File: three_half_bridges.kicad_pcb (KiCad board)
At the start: 2 copper layers, 100 x 100 mm, 167 parts, among them J1 Conn_01x06_Pin, J2 Conn_01x06_Pin, J3 Conn_01x06_Pin, J4 Current Sense, J5 Conn_01x01_Socket, J6 Conn_01x01_Socket, J7 Conn_01x01_Socket, J8 Conn_01x01_Socket, J9 Conn_01x01_Socket, Q1 Q_NMOS_GDS, Q2 Q_NMOS_GDS, Q3 Q_NIGBT_GCE, Q4 Q_NIGBT_GCE, Q5 Q_NIGBT_GCE, Q6 Q_NIGBT_GCE, Q7 Q_NIGBT_GCE, Q8 Q_NIGBT_GCE, U1 ACS730xLCTR-50AB, U10 ADuM121N, U13 EL7202CN, U14 EL7202CN, U15 EL7202CN, U16 EL7202CN, U17 ACS730xLCTR-50AB, U18 ADuM121N, U19 ADuM121N, U2 ACS730xLCTR-50AB, U22 EL7202CN, U23 EL7202CN, U3 SN6505BDBV, U4 ADuM121N, U5 ADuM121N, U9 ADuM121N

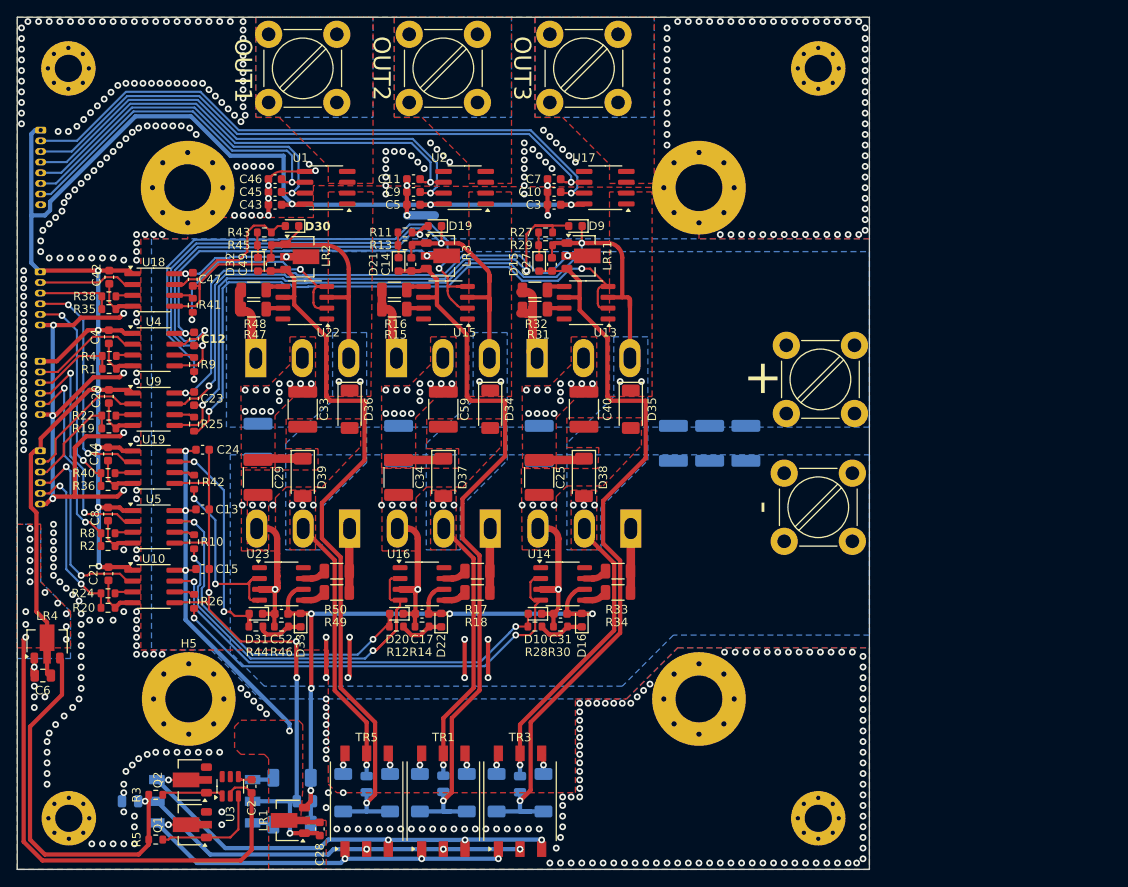
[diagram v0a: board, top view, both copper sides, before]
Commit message: Updated LDO footrprint to use the SOT89 LM78L05 (issue 10); moved high side local regulators closer to digital isolator ICs (issue 10); pushed digital isolator ICs further to the allow room for LRs (issue 10); changed designator letter for zener diodes to Z to make it easier when hand soldering (issue 5) Updated footprints from placeholders (most of the diodes) to actual real component choices updated resistor values for BOM consolidation (220, 1k) moved resistor related to PGOOD for more optimal routing w/ minimal impact to function Changed structure of isolated driver design to use voltage doubler and 6505 or similar IC directly (issue 7,8,13) Only 5VDC is required for low voltage side, although several amps may be required depending on gate drive requirements Updated transformer footprint for more common 7.5mm by 2.5mm spacing, several 1:1.1 to 1:1.5 transformers are avilable with such spacing (issue 7) Moved Q8 designator back to correct place along with others that were mislocated somehow... Fixed placement of some footprints that were slightly off or not aligned to 0.25mm grid Replaced specific SO8 MOSFET driver with choose-your-own generic. I am personally using some cheapo LCSC TI 27523 clones (issue 11) added EVEN MORE VIAS!!!! thermal vias on not current sensitive pins to make soldering easier Added artwork (issue 6)
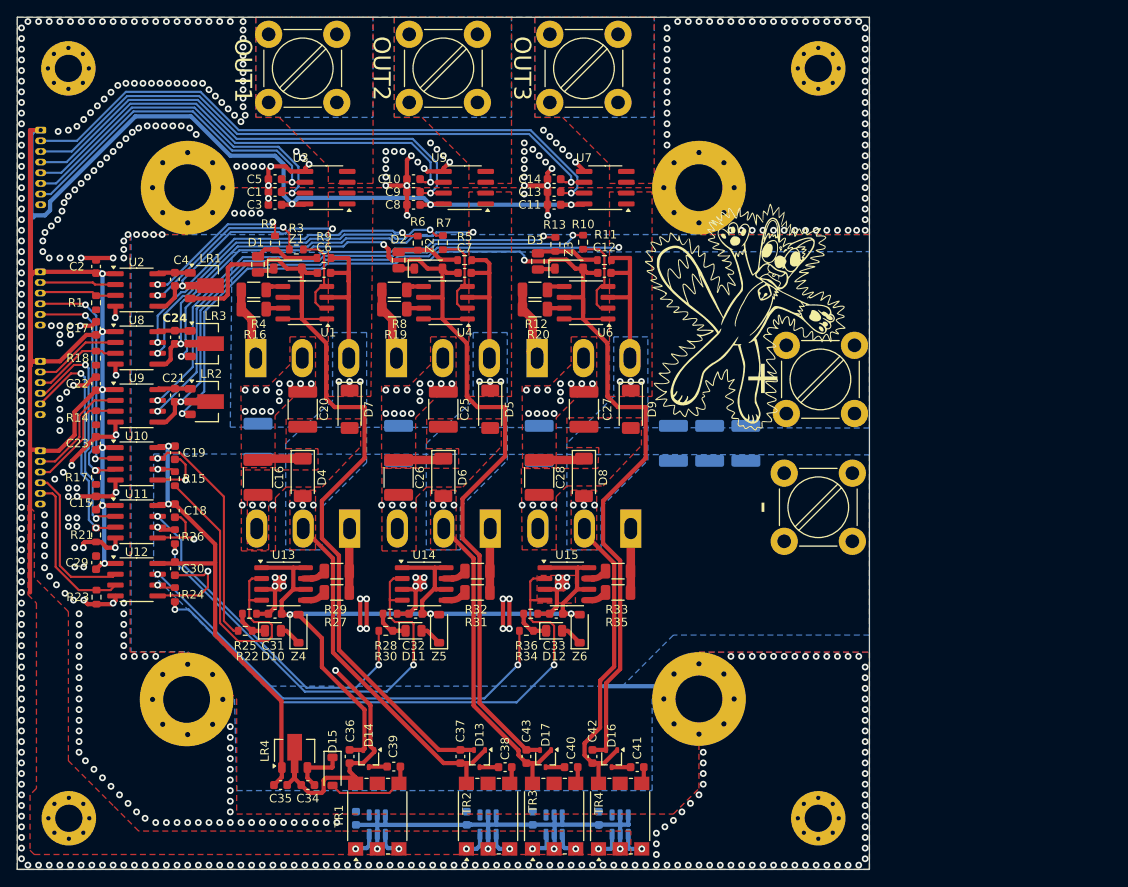
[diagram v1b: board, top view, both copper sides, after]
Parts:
- removed the C1 at (93.2, 122.0)
- removed the C16 at (130.0, 120.0)
- removed the C2 at (107.5, 120.2)
- removed the C26 at (113.8, 122.0)
- removed the C28 at (115.5, 125.2)
- removed the C30 at (139.0, 120.0)
- removed the C6 at (83.0, 107.2)
- removed D18, D28, D29: 1N4148WT, Diode_SMD:D_SOD-128
- removed the D7 at (112.2, 124.8)
- removed the D8 at (112.2, 119.2)
- removed LR11: AMS1117-5.0, Package_TO_SOT_SMD:SOT-89-3
- removed the Q1 at (100.2, 124.8)
- removed the Q2 at (100.2, 119.5)
- removed the R22 at (90.8, 76.8)
- removed the R24 at (90.7, 97.6)
- removed the R3 at (96.2, 121.2)
- removed R38, R40: 470, Resistor_SMD:R_0603_1608Metric
- removed the R4 at (90.8, 69.8)
- removed the R5 at (96.2, 126.5)
- removed the R8 at (90.7, 90.5)
- removed the TR2 at (102.0, 122.0)
- removed U23: EL7202CN, Package_SO:SO-8_3.9x4.9mm_P1.27mm
- removed the U3 at (105.0, 120.2)
- added C34: 1u, Capacitor_SMD:C_0603_1608Metric, F.Cu at (114.1, 120.1)
- added C35: 1u, Capacitor_SMD:C_0603_1608Metric, F.Cu at (110.9, 120.1)
- added C36: 1u, Capacitor_SMD:C_0603_1608Metric, F.Cu at (119.0, 116.8)
- added C37: 1u, Capacitor_SMD:C_0603_1608Metric, F.Cu at (132.0, 116.8)
- added C38: 1u, Capacitor_SMD:C_0603_1608Metric, F.Cu at (137.2, 118.0)
- added C39: 1u, Capacitor_SMD:C_0603_1608Metric, F.Cu at (124.2, 117.9)
- added C40: 1u, Capacitor_SMD:C_0603_1608Metric, F.Cu at (145.0, 118.0)
- added C41: 1u, Capacitor_SMD:C_0603_1608Metric, F.Cu at (152.8, 118.0)
- added C42: 1u, Capacitor_SMD:C_0603_1608Metric, F.Cu at (147.5, 116.8)
- added C43: 1u, Capacitor_SMD:C_0603_1608Metric, F.Cu at (139.8, 116.8)
- added C50: 1u, Capacitor_SMD:C_0603_1608Metric, B.Cu at (140.5, 124.0)
- added C52: 1u, Capacitor_SMD:C_0603_1608Metric, B.Cu at (119.8, 124.0)
- added C53: 1u, Capacitor_SMD:C_0603_1608Metric, B.Cu at (132.8, 124.0)
- added D15: D_Schottky, Diode_SMD:D_SOD-123, F.Cu at (117.0, 118.5)
- added D16: BAT54SW, Package_TO_SOT_SMD:SOT-323_SC-70, F.Cu at (149.8, 117.0)
- added G***: LOGO, PM art:PM_art, F.Cu at (165.6, 65.2)
- added TR1: EPC3668G, Transformer_SMD:Pulse_PA2004NL, F.Cu at (122.2, 123.8)
- added U13: SO8 GATE DRVR, Package_SO:SO-8_3.9x4.9mm_P1.27mm, F.Cu at (111.2, 96.5)
- added U15: SO8 GATE DRVR, Package_SO:SO-8_3.9x4.9mm_P1.27mm, F.Cu at (144.5, 96.5)
- added U17: SN6505BDBV, Package_TO_SOT_SMD:SOT-23-6, B.Cu at (150.8, 124.8)
- added U18: SN6505BDBV, Package_TO_SOT_SMD:SOT-23-6, B.Cu at (135.2, 124.8)
- added U19: SN6505BDBV, Package_TO_SOT_SMD:SOT-23-6, B.Cu at (122.2, 124.8)
- C1: renamed from C45; value 100n -> 1n
- C10: renamed from C11; value 100n -> 1n
- C12: renamed from C27; value 100n -> 1u
- C13: renamed from C10; value 100n -> 1n
- C14: renamed from C7; value 100n -> 1n
- C16: renamed from C29; value 100n -> 470n
- C20: renamed from C33; value 100n -> 470n
- C25: renamed from C59; value 100n -> 470n
- C26: renamed from C34; value 100n -> 470n
- C27: renamed from C40; value 100n -> 470n
- C28: renamed from C25; value 100n -> 470n
- C5: renamed from C46; value 100n -> 1n
- C51: value 10u -> 1u; footprint Capacitor_SMD:C_0805_2012Metric -> Capacitor_SMD:C_0603_1608Metric
- C6: renamed from C49; value 100n -> 1u
- C7: renamed from C14; value 100n -> 1u
- C9: value 100n -> 1n
- D1: renamed from D30; footprint LED_SMD:LED_0603_1608Metric -> Capacitor_SMD:C_0805_2012Metric
- D10: renamed from D31; footprint LED_SMD:LED_0603_1608Metric -> LED_SMD:LED_0805_2012Metric
- D11: renamed from D20; footprint LED_SMD:LED_0603_1608Metric -> LED_SMD:LED_0805_2012Metric
- D12: renamed from D10; footprint LED_SMD:LED_0603_1608Metric -> LED_SMD:LED_0805_2012Metric
- D13, D14, D17: value 1N4148WT -> BAT54SW; footprint Diode_SMD:D_SOD-128 -> Package_TO_SOT_SMD:SOT-323_SC-70; moved to F.Cu
- D2: renamed from D19; footprint LED_SMD:LED_0603_1608Metric -> Capacitor_SMD:C_0805_2012Metric
- D3: renamed from D9; footprint LED_SMD:LED_0603_1608Metric -> Capacitor_SMD:C_0805_2012Metric
- D4: renamed from D39; value 1N4148WT -> FAST 1A DIODE
- D5: renamed from D34; value 1N4148WT -> FAST 1A DIODE
- D6: renamed from D37; value 1N4148WT -> FAST 1A DIODE
- D7: renamed from D36; value 1N4148WT -> FAST 1A DIODE
- D8: renamed from D38; value 1N4148WT -> FAST 1A DIODE
- D9: renamed from D35; value 1N4148WT -> FAST 1A DIODE
- LR1, LR2, LR3, LR4: value AMS1117-5.0 -> MC78L08_SOT89
- R1: renamed from R35; value 10k -> 1k
- R11: renamed from R27; value 4.7k -> 1k
- R14: renamed from R19; value 10k -> 1k
- R17: renamed from R36; value 10k -> 1k
- R18: renamed from R1; value 10k -> 1k
- R21: renamed from R2; value 10k -> 1k
- R23: renamed from R20; value 10k -> 1k
- R25: renamed from R44; value 4.7k -> 1k
- R30: renamed from R12; value 4.7k -> 1k
- R34: renamed from R28; value 4.7k -> 1k
- R5: renamed from R11; value 4.7k -> 1k
- R9: renamed from R43; value 4.7k -> 1k
- TR2: renamed from TR5; value Wuerth_750315371 -> EPC3668G; footprint Transformer_SMD:Transformer_Wuerth_750315371 -> Transformer_SMD:Pulse_PA2004NL
- TR3: renamed from TR1; value Wuerth_750315371 -> EPC3668G; footprint Transformer_SMD:Transformer_Wuerth_750315371 -> Transformer_SMD:Pulse_PA2004NL
- TR4: renamed from TR3; value Wuerth_750315371 -> EPC3668G; footprint Transformer_SMD:Transformer_Wuerth_750315371 -> Transformer_SMD:Pulse_PA2004NL
- U1: renamed from U22; value EL7202CN -> SO8 GATE DRVR
- U14: value EL7202CN -> SO8 GATE DRVR
- U16: value EL7202CN -> SN6505BDBV; footprint Package_SO:SO-8_3.9x4.9mm_P1.27mm -> Package_TO_SOT_SMD:SOT-23-6; moved to B.Cu
- U4: renamed from U15; value EL7202CN -> SO8 GATE DRVR
- U6: renamed from U13; value EL7202CN -> SO8 GATE DRVR
- Z1: renamed from D32; footprint Diode_SMD:D_0603_1608Metric -> Diode_SMD:D_SOD-123
- Z2: renamed from D21; footprint Diode_SMD:D_0603_1608Metric -> Diode_SMD:D_SOD-123
- Z3: renamed from D15; footprint Diode_SMD:D_0603_1608Metric -> Diode_SMD:D_SOD-123
- Z4: renamed from D33; footprint Diode_SMD:D_0603_1608Metric -> Diode_SMD:D_SOD-123
- Z5: renamed from D22; footprint Diode_SMD:D_0603_1608Metric -> Diode_SMD:D_SOD-123
- Z6: renamed from D16; footprint Diode_SMD:D_0603_1608Metric -> Diode_SMD:D_SOD-123
- moved LR1 63.5 mm to (102.2, 61.5), turned to 0 degrees
- moved R10 50.4 mm to (146.4, 56.4)
- moved R7 32.5 mm to (129.9, 56.5)
- moved U16 32.2 mm to (143.0, 124.8), turned to 90 degrees
- moved LR4 31.8 mm to (112.5, 116.1)
- moved LR3 29.6 mm to (102.2, 68.3)
- moved C51 27.5 mm to (148.2, 124.0)
- moved D14 20.9 mm to (121.2, 117.0), turned to -90 degrees
- moved LR2 20.3 mm to (102.2, 75.1)
- moved U14 16.2 mm to (127.8, 96.5)
- moved D17 15.3 mm to (142.0, 117.0), turned to -90 degrees
- moved TR2 14.4 mm to (135.2, 123.8)
- moved R3 13.8 mm to (112.8, 57.2), turned to 180 degrees
- moved TR3 13.1 mm to (143.0, 123.8)
- moved TR4 11.9 mm to (150.8, 123.8)
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- renumbered C3 to C11, C8 to C15, C4 to C17, C13 to C18, C24 to C19, C42 to C2, C23 to C21, C20 to C22, C44 to C23, C12 to C24, C21 to C29, C43 to C3, C15 to C30, C52 to C31, C17 to C32, C31 to C33, C47 to C4, C18 to C44, C19 to C45, C32 to C46, C22 to C47, C35 to C48, C36 to C49, C5 to C8, J9 to J1, J8 to J2, J7 to J3, J5 to J4, J6 to J5, J4 to J6, J3 to J7, J2 to J8, J1 to J9, Q5 to Q1, Q3 to Q2, Q7 to Q3, Q6 to Q4, Q4 to Q5, Q8 to Q6, R25 to R10, R32 to R12, R29 to R13, R42 to R15, R47 to R16, R15 to R19, R45 to R2, R31 to R20, R46 to R22, R26 to R24, R10 to R26, R49 to R27, R14 to R28, R50 to R29, R41 to R3, R18 to R31, R17 to R32, R34 to R35, R30 to R36, R48 to R4, R13 to R6, R9 to R7, R16 to R8, U19 to U10, U5 to U11, U10 to U12, U18 to U2, U1 to U3, U2 to U5, U17 to U7, U4 to U8
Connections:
- C12 pad 1: Net-(D13-K) -> Net-(D3-K)
- C12 pad 2: Net-(D35-K) -> /half bridge 1/SWNODE
- C21 pad 1: Net-(LR11-VO) -> Net-(LR11-OUT)
- C21 pad 2: Net-(D35-K) -> /half bridge 1/SWNODE
- C24 pad 1: Net-(LR3-VO) -> Net-(LR8-OUT)
- C24 pad 2: Net-(D19-K) -> /half bridge 2/SWNODE
- C4 pad 1: Net-(LR2-VO) -> Net-(LR12-OUT)
- C4 pad 2: Net-(D30-K) -> /half bridge 3/SWNODE
- C51 pad 1: Net-(D30-K) -> GND
- C51 pad 2: Net-(D28-K) -> +5V
- C6 pad 1: Net-(D28-K) -> Net-(D4-K)
- C6 pad 2: Net-(D30-K) -> /half bridge 3/SWNODE
- C7 pad 1: Net-(D17-K) -> Net-(D2-K)
- C7 pad 2: Net-(D19-K) -> /half bridge 2/SWNODE
- D10 pad 1: -VDC -> Net-(D31-K)
- D11 pad 1: -VDC -> Net-(D20-K)
- D12 pad 1: -VDC -> Net-(D10-K)
- D13 pad 1: Net-(D13-K) -> /half bridge 3/SWNODE
- D13 pad 2: Net-(D13-A) -> Net-(D4-K)
- D14 pad 1: Net-(D13-K) -> -VDC
- D14 pad 2: Net-(D14-A) -> 12V_HV
- D17 pad 1: Net-(D17-K) -> /half bridge 2/SWNODE
- D17 pad 2: Net-(D17-A) -> Net-(D2-K)
- D3 pad 1: Net-(D35-K) -> Net-(D9-K)
- D4 pad 2: Net-(D30-K) -> /half bridge 3/SWNODE
- D5 pad 1: Net-(D19-K) -> /half bridge 2/SWNODE
- D6 pad 2: Net-(D19-K) -> /half bridge 2/SWNODE
- D7 pad 1: Net-(D30-K) -> /half bridge 3/SWNODE
- D8 pad 2: Net-(D35-K) -> /half bridge 1/SWNODE
- D9 pad 1: Net-(D35-K) -> /half bridge 1/SWNODE
- LR1 pad 1: -VDC -> Net-(LR12-OUT)
- LR1 pad 2: 5V_HV -> /half bridge 3/SWNODE
- LR1 pad 3: 12V_HV -> Net-(D4-K)
- LR2 pad 1: Net-(D30-K) -> Net-(LR11-OUT)
- LR2 pad 2: Net-(LR2-VO) -> /half bridge 1/SWNODE
- LR2 pad 3: Net-(D28-K) -> Net-(D3-K)
- LR3 pad 1: Net-(D19-K) -> Net-(LR8-OUT)
- LR3 pad 2: Net-(LR3-VO) -> /half bridge 2/SWNODE
- LR3 pad 3: Net-(D17-K) -> Net-(D2-K)
- LR4 pad 1: GND -> 5V_HV
- LR4 pad 2: +5V -> -VDC
- LR4 pad 3: +15V -> Net-(D5-K)
- Q1 pad 3: Net-(D35-K) -> /half bridge 1/SWNODE
- Q2 pad 3: Net-(D19-K) -> /half bridge 2/SWNODE
- Q3 pad 3: Net-(D30-K) -> /half bridge 3/SWNODE
- Q4 pad 2: Net-(D35-K) -> /half bridge 1/SWNODE
- Q5 pad 2: Net-(D19-K) -> /half bridge 2/SWNODE
- Q6 pad 2: Net-(D30-K) -> /half bridge 3/SWNODE
- R11 pad 1: Net-(D15-K) -> Net-(D9-K)
- R11 pad 2: Net-(D9-A) -> /half bridge 1/SWNODE
- R13 pad 1: Net-(D15-K) -> Net-(U9-VIA)
- R13 pad 2: Net-(D35-K) -> Net-(D9-K)
- R2 pad 1: Net-(D32-K) -> Net-(U18-VIA)
- R22 pad 1: Net-(D33-K) -> Net-(D31-K)
- R24 pad 1: Net-(U14-IN_A) (its old number) -> Net-(U12-IN_A)
- R25 pad 1: Net-(D33-K) -> Net-(D31-K)
- R25 pad 2: Net-(D31-A) -> Net-(U19-VIA)
- R26 pad 1: Net-(U16-IN_A) -> Net-(U11-IN_A)
- R28 pad 1: Net-(D22-K) -> Net-(D20-K)
- R30 pad 1: Net-(D22-K) -> Net-(D20-K)
- R30 pad 2: Net-(D20-A) -> Net-(U5-VIA)
- R31 pad 2: Net-(U16-OUT_B) -> Net-(U11-OUT_B)
- R32 pad 2: Net-(U16-OUT_A) -> Net-(U11-OUT_A)
- R33 pad 2: Net-(U14-OUT_A) (its old number) -> Net-(U12-OUT_A)
- R34 pad 1: Net-(D16-K) -> Net-(D10-K)
- R34 pad 2: Net-(D10-A) -> Net-(U10-VIA)
- R35 pad 2: Net-(U14-OUT_B) (its old number) -> Net-(U12-OUT_B)
- R36 pad 1: Net-(D16-K) -> Net-(D10-K)
- R5 pad 1: Net-(D21-K) -> Net-(D19-K)
- R5 pad 2: Net-(D19-A) -> /half bridge 2/SWNODE
- R6 pad 1: Net-(D21-K) -> Net-(U4-VIA)
- R9 pad 1: Net-(D32-K) -> Net-(D30-K)
- R9 pad 2: Net-(D30-A) -> /half bridge 3/SWNODE
- TR2 pad 1: PRI1 -> Net-(U7-D2)
- TR2 pad 2: +15V -> +5V
- TR2 pad 3: PRI2 -> Net-(U7-D1)
- TR2 pad 5: Net-(D30-K) -> unconnected-(TR5-Pad5)
- TR2 pad 6: Net-(D28-A) -> /half bridge 3/SWNODE
- TR3 pad 1: PRI1 -> Net-(U3-D2)
- TR3 pad 2: +15V -> +5V
- TR3 pad 3: PRI2 -> Net-(U3-D1)
- TR3 pad 5: Net-(D19-K) -> unconnected-(TR1-Pad5)
- TR3 pad 6: Net-(D17-A) -> /half bridge 2/SWNODE
- TR4 pad 1: PRI1 -> Net-(U6-D2)
- TR4 pad 2: +15V -> +5V
- TR4 pad 3: PRI2 -> Net-(U6-D1)
- TR4 pad 4: Net-(D14-A) -> Net-(C39-Pad1)
- TR4 pad 5: Net-(D35-K) -> unconnected-(TR3-Pad5)
- TR4 pad 6: Net-(D13-A) -> /half bridge 1/SWNODE
- U1 pad 1: unconnected-(U22-NC-Pad1) -> Net-(D4-K)
- U1 pad 3: Net-(D30-K) -> /half bridge 3/SWNODE
- U1 pad 6: Net-(D28-K) -> Net-(D4-K)
- U1 pad 8: unconnected-(U22-NC-Pad8) -> Net-(D4-K)
- U10 pad 3: Net-(U19-VIB) -> /half bridge 3/LO_{IN}
- U10 pad 7: Net-(D31-A) -> Net-(U19-VIA)
- U11 pad 3: Net-(U5-VIB) -> /half bridge 2/LO_{IN}
- U11 pad 7: Net-(D20-A) -> Net-(U5-VIA)
- U12 pad 3: Net-(U10-VIB) -> /half bridge 1/LO_{IN}
- U12 pad 7: Net-(D10-A) -> Net-(U10-VIA)
- U14 pad 1: unconnected-(U14-NC-Pad1) -> 12V_HV
- U14 pad 2: Net-(U14-IN_A) (its old number) -> Net-(U11-IN_A)
- U14 pad 4: Net-(U14-IN_A) (its old number) -> Net-(U11-IN_A)
- U14 pad 5: Net-(U14-OUT_B) (its old number) -> Net-(U11-OUT_B)
- U14 pad 7: Net-(U14-OUT_A) (its old number) -> Net-(U11-OUT_A)
- U14 pad 8: unconnected-(U14-NC-Pad8) -> 12V_HV
- U16 pad 1: unconnected-(U16-NC-Pad1) -> Net-(U3-D1)
- U16 pad 2: Net-(U16-IN_A) -> +5V
- U16 pad 3: -VDC -> Net-(U3-D2)
- U16 pad 4: Net-(U16-IN_A) -> GND
- U16 pad 5: Net-(U16-OUT_B) -> +5V
- U16 pad 6: 12V_HV -> +5V
- U2 pad 3: Net-(U18-VIB) -> /half bridge 3/HI_{IN}
- U2 pad 5: Net-(D30-K) -> /half bridge 3/SWNODE
- U2 pad 7: Net-(D30-A) -> Net-(U18-VIA)
- U2 pad 8: Net-(LR2-VO) -> Net-(LR12-OUT)
- U3 pad 1: Net-(D30-K) -> /half bridge 3/SWNODE
- U3 pad 2: Net-(D30-K) -> /half bridge 3/SWNODE
- U4 pad 1: unconnected-(U15-NC-Pad1) -> Net-(D2-K)
- U4 pad 3: Net-(D19-K) -> /half bridge 2/SWNODE
- U4 pad 6: Net-(D17-K) -> Net-(D2-K)
- U4 pad 8: unconnected-(U15-NC-Pad8) -> Net-(D2-K)
- U5 pad 1: Net-(D19-K) -> /half bridge 2/SWNODE
- U5 pad 2: Net-(D19-K) -> /half bridge 2/SWNODE
- U6 pad 1: unconnected-(U13-NC-Pad1) -> Net-(D3-K)
- U6 pad 3: Net-(D35-K) -> /half bridge 1/SWNODE
- U6 pad 6: Net-(D13-K) -> Net-(D3-K)
- U6 pad 8: unconnected-(U13-NC-Pad8) -> Net-(D3-K)
- U7 pad 1: Net-(D35-K) -> /half bridge 1/SWNODE
- U7 pad 2: Net-(D35-K) -> /half bridge 1/SWNODE
- U8 pad 3: Net-(U4-VIB) -> /half bridge 2/HI_{IN}
- U8 pad 5: Net-(D19-K) -> /half bridge 2/SWNODE
- U8 pad 7: Net-(D19-A) -> Net-(U4-VIA)
- U8 pad 8: Net-(LR3-VO) -> Net-(LR8-OUT)
- U9 pad 3: Net-(U9-VIB) -> /half bridge 1/HI_{IN}
- U9 pad 5: Net-(D35-K) -> /half bridge 1/SWNODE
- U9 pad 7: Net-(D9-A) -> Net-(U9-VIA)
- U9 pad 8: Net-(LR11-VO) -> Net-(LR11-OUT)
- Z1 pad 1: Net-(D32-K) -> Net-(D30-A)
- Z1 pad 2: Net-(D28-K) -> Net-(D4-K)
- Z2 pad 1: Net-(D21-K) -> Net-(D19-A)
- Z2 pad 2: Net-(D17-K) -> Net-(D2-K)
- Z3 pad 1: Net-(D15-K) -> Net-(D9-A)
- Z3 pad 2: Net-(D13-K) -> Net-(D3-K)
- Z4 pad 1: Net-(D33-K) -> Net-(D31-A)
- Z5 pad 1: Net-(D22-K) -> Net-(D20-A)
- Z6 pad 1: Net-(D16-K) -> Net-(D10-A)
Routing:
- net Net-(D3-K): track 0.00 -> 141.6 mm, vias 0 -> 2
- net Net-(D35-K): track 134.0 -> 0.00 mm, vias 8 -> 0
- net /half bridge 1/SWNODE: track 0.00 -> 125.8 mm, vias 0 -> 8
- net Net-(D2-K): track 0.00 -> 120.0 mm, vias 0 -> 2
- net Net-(D19-K): track 116.6 -> 7.61 mm, vias 8 -> 0
- net /half bridge 2/SWNODE: track 0.00 -> 104.3 mm, vias 0 -> 8
- net Net-(D4-K): track 0.00 -> 102.7 mm
- net Net-(D13-K): track 92.6 -> 0.00 mm, vias 1 -> 0
- net +15V: track 92.4 -> 0.00 mm, vias 4 -> 0
- net /half bridge 3/SWNODE: track 0.00 -> 88.7 mm, vias 0 -> 8
- net Net-(D28-K): track 87.0 -> 0.00 mm, vias 1 -> 0
- net Net-(D17-K): track 86.6 -> 0.00 mm, vias 1 -> 0
- net Net-(D30-K): track 79.5 -> 7.67 mm, vias 6 -> 0
- net Net-(U12-IN_A): track 0.00 -> 67.4 mm, vias 0 -> 2
- net Net-(D9-A): track 68.3 -> 1.67 mm, vias 2 -> 0
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- added copper zone on B.Cu, net /half bridge 1/SWNODE
- added copper zone on F.Cu, net /half bridge 1/SWNODE
- added copper zone on B.Cu, net /half bridge 2/SWNODE
- added copper zone on F.Cu, net /half bridge 2/SWNODE
- added copper zone on B.Cu, net /half bridge 3/SWNODE
- added copper zone on F.Cu, net /half bridge 3/SWNODE
- removed copper zone on B.Cu, net +5V
- removed copper zone on F.Cu, net 5V_HV
- removed copper zone on B.Cu, net Net-(D19-K)
- removed copper zone on F.Cu, net Net-(D19-K)
- removed copper zone on B.Cu, net Net-(D30-K)
- removed copper zone on F.Cu, net Net-(D30-K)
- removed copper zone on B.Cu, net Net-(D35-K)
- removed copper zone on F.Cu, net Net-(D35-K)

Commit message: moved silkscreen for HVDC input and added additional 5VDC for the low voltage primary input
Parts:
- renumbered C52 to C1, C13 to C10, C10 to C11, C24 to C12, C18 to C13, C7 to C14, C30 to C15, C43 to C16, C32 to C17, C44 to C18, C45 to C19, C34 to C2, C22 to C20, C29 to C21, C47 to C22, C21 to C23, C19 to C24, C28 to C25, C36 to C26, C12 to C27, C35 to C28, C16 to C29, C11 to C3, C42 to C30, C33 to C31, C46 to C32, C20 to C33, C26 to C34, C48 to C35, C49 to C36, C39 to C37, C40 to C38, C41 to C39, C17 to C4, C27 to C40, C38 to C41, C2 to C42, C3 to C43, C23 to C44, C1 to C45, C5 to C46, C4 to C47, C50 to C48, C6 to C49, C8 to C5, C51 to C50, C37 to C51, C31 to C52, C25 to C59, C14 to C7, C15 to C8, D14 to D1, D12 to D10, D2 to D19, D17 to D2, D11 to D20, D16 to D3, D1 to D30, D10 to D31, D5 to D34, D9 to D35, D7 to D36, D6 to D37, D8 to D38, D4 to D39, D13 to D4, D15 to D5, D3 to D9, J9 to J1, J8 to J2, J7 to J3, J6 to J4, J4 to J5, J5 to J6, J3 to J7, J2 to J8, J1 to J9, LR2 to LR11, LR1 to LR12, LR4 to LR7, LR3 to LR8, Q2 to Q3, Q5 to Q4, Q1 to Q5, Q4 to Q6, Q3 to Q7, Q6 to Q8, R18 to R1, R26 to R10, R5 to R11, R30 to R12, R6 to R13, R28 to R14, R19 to R15, R8 to R16, R32 to R17, R31 to R18, R14 to R19, R21 to R2, R23 to R20, R10 to R25, R24 to R26, R11 to R27, R34 to R28, R13 to R29, R36 to R30, R20 to R31, R12 to R32, R35 to R34, R1 to R35, R17 to R36, R3 to R41, R15 to R42, R9 to R43, R25 to R44, R2 to R45, R22 to R46, R16 to R47, R4 to R48, R27 to R49, R29 to R50, R7 to R9, TR3 to TR1, TR1 to TR2, TR4 to TR3, TR2 to TR5, U3 to U1, U12 to U10, U14 to U11, U15 to U12, U6 to U13, U13 to U14, U4 to U15, U7 to U17, U2 to U18, U10 to U19, U5 to U2, U1 to U22, U16 to U3, U8 to U4, U11 to U5, U17 to U6, U18 to U7, U19 to U8, Z3 to Z1, Z6 to Z2, Z2 to Z21, Z5 to Z22, Z1 to Z32, Z4 to Z33
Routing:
- net GND: track 87.9 -> 100.0 mm, vias 513 -> 511
- net /half bridge 3/OUT: vias 0 -> 7
- net /half bridge 2/OUT: vias 0 -> 7
- net /half bridge 1/OUT: vias 0 -> 7
- net -VDC: vias 36 -> 33
- net +VDC: vias 39 -> 29
- added copper zone on In2.Cu, net +VDC
- added copper zone on In2.Cu, net -VDC
- added copper zone on In1.Cu, net /half bridge 1/OUT
- added copper zone on In1.Cu, net /half bridge 1/SWNODE
- added copper zone on In1.Cu, net /half bridge 2/OUT
- added copper zone on In1.Cu, net /half bridge 2/SWNODE
- added copper zone on In1.Cu, net /half bridge 3/OUT
- added copper zone on In1.Cu, net /half bridge 3/SWNODE
- added copper zone on In1.Cu, net GND
- added copper zone on In2.Cu, net GND
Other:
- copper layers 2 -> 4

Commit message: forgot to save and close prior to last commit
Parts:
- added J10: Conn_01x02_Pin, Connector_JST:JST_XH_B2B-XH-AM_1x02_P2.50mm_Vertical, F.Cu at (100.0, 126.2)
- moved G*** 1.77 mm to (165.3, 67.0)
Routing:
- net GND: vias 511 -> 508
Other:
- board text added: "5VDC"
- board text added: "GND"

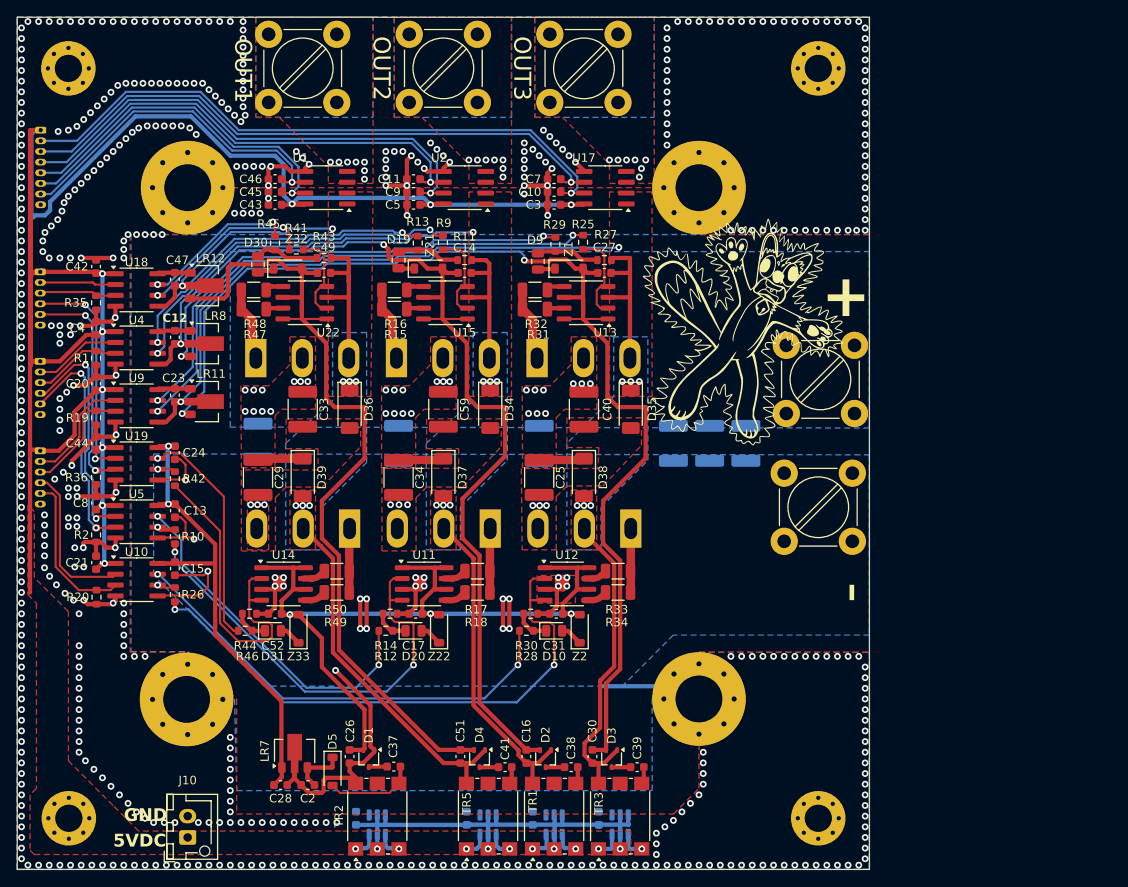
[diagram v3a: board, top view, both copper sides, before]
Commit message: updated footprint for terminal blocks to use AMT0450028DB0000G‎
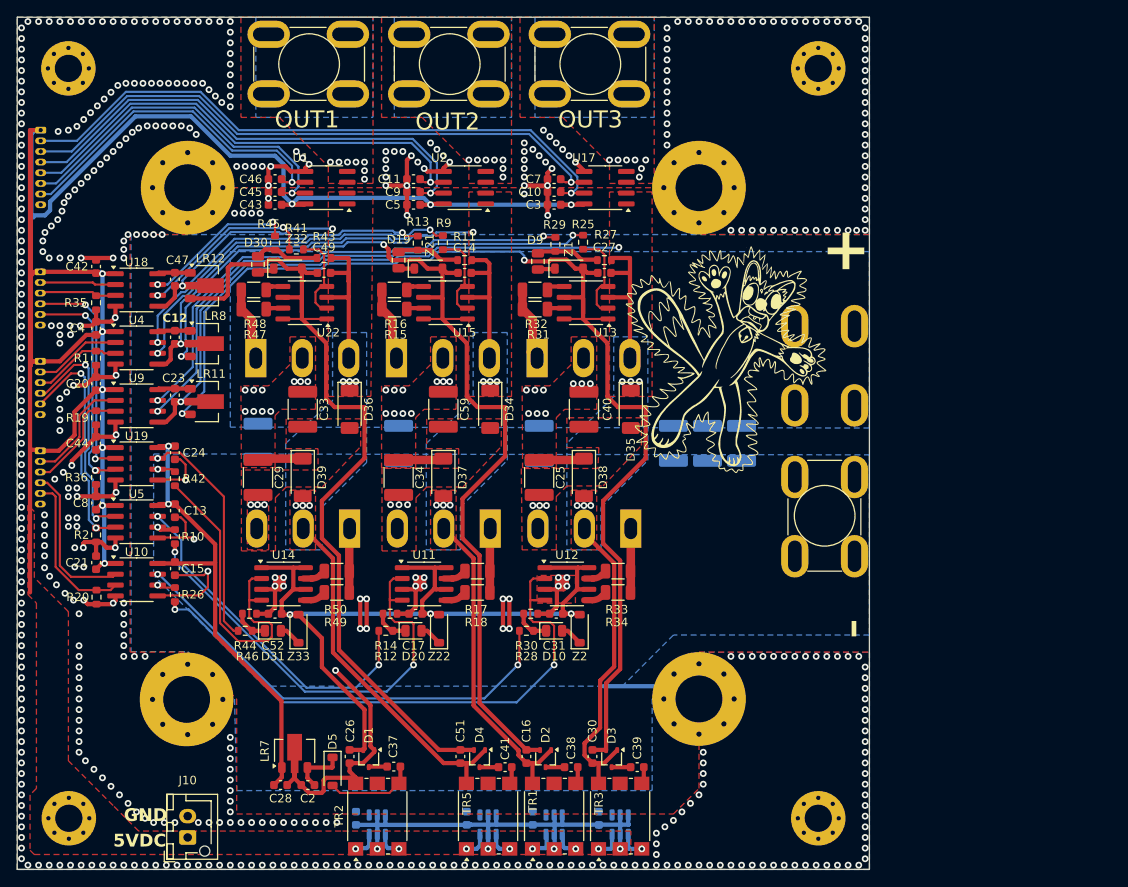
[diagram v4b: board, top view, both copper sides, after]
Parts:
- J5: footprint TerminalBlock_MetzConnect:TerminalBlock_MetzConnect_360425_1x01_Horizontal_ScrewM4.0_Boxed -> Library:AMT0450028DB0000G; moved to B.Cu
- J6, J7, J8, J9: footprint TerminalBlock_MetzConnect:TerminalBlock_MetzConnect_360425_1x01_Horizontal_ScrewM4.0_Boxed -> Library:AMT0450028DB0000G
- moved J6 9.83 mm to (171.2, 93.2), turned to 90 degrees
- moved G*** 3.82 mm to (163.3, 70.2)
- moved J5 2.46 mm to (171.2, 66.2), turned to -90 degrees
- moved C18 0.50 mm to (165.0, 80.0)
- moved C19 0.25 mm to (161.0, 80.0)
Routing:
- net GND: vias 508 -> 501

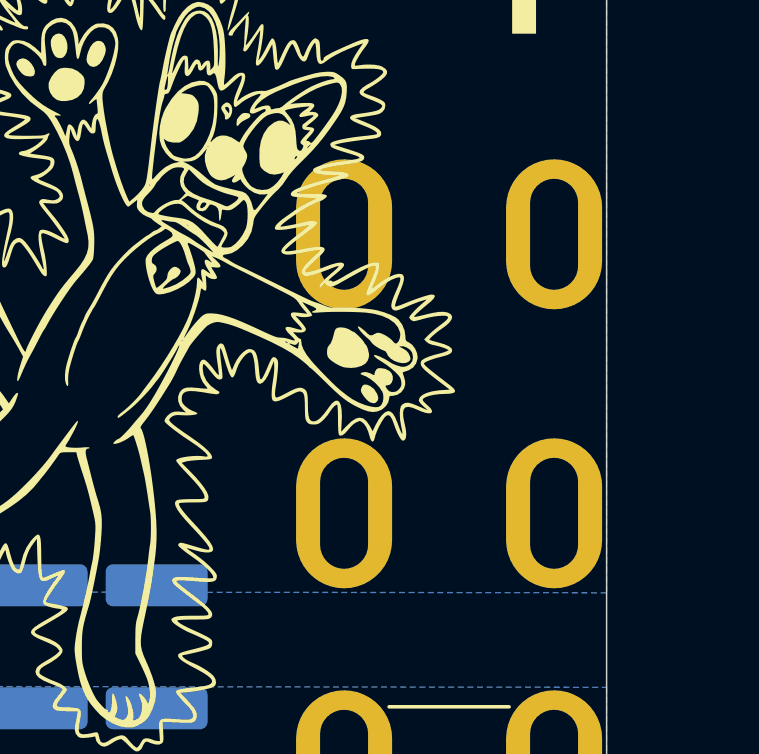
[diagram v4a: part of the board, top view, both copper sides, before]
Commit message: fixed the accidentally flipped terminal block posistive terminal
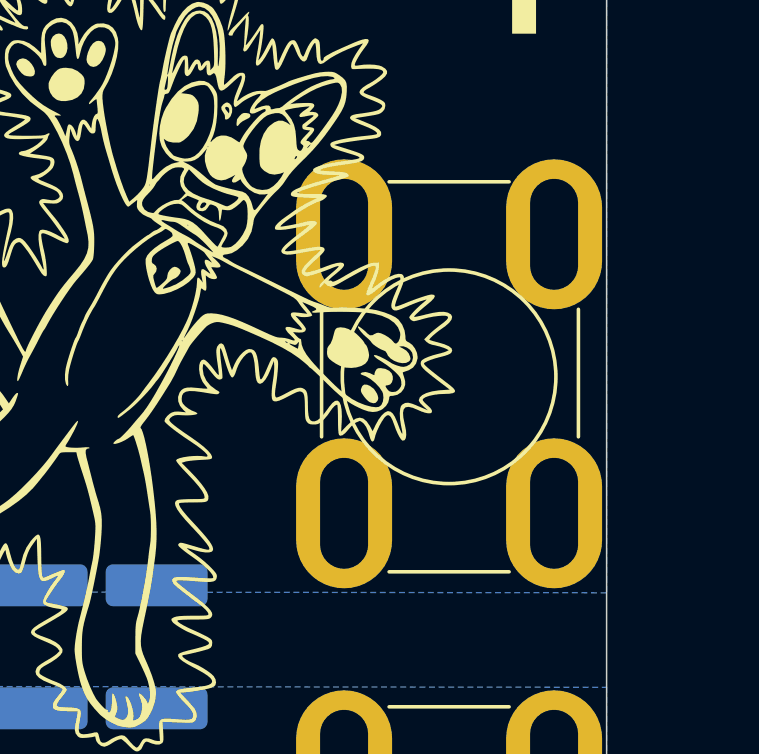
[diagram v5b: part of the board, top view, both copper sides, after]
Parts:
- J5: moved to F.Cu
- moved J5 7.00 mm to (178.2, 66.2)
